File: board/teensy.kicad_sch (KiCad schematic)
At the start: 1 part, among them U2 Teensy4.1_DEV-16771

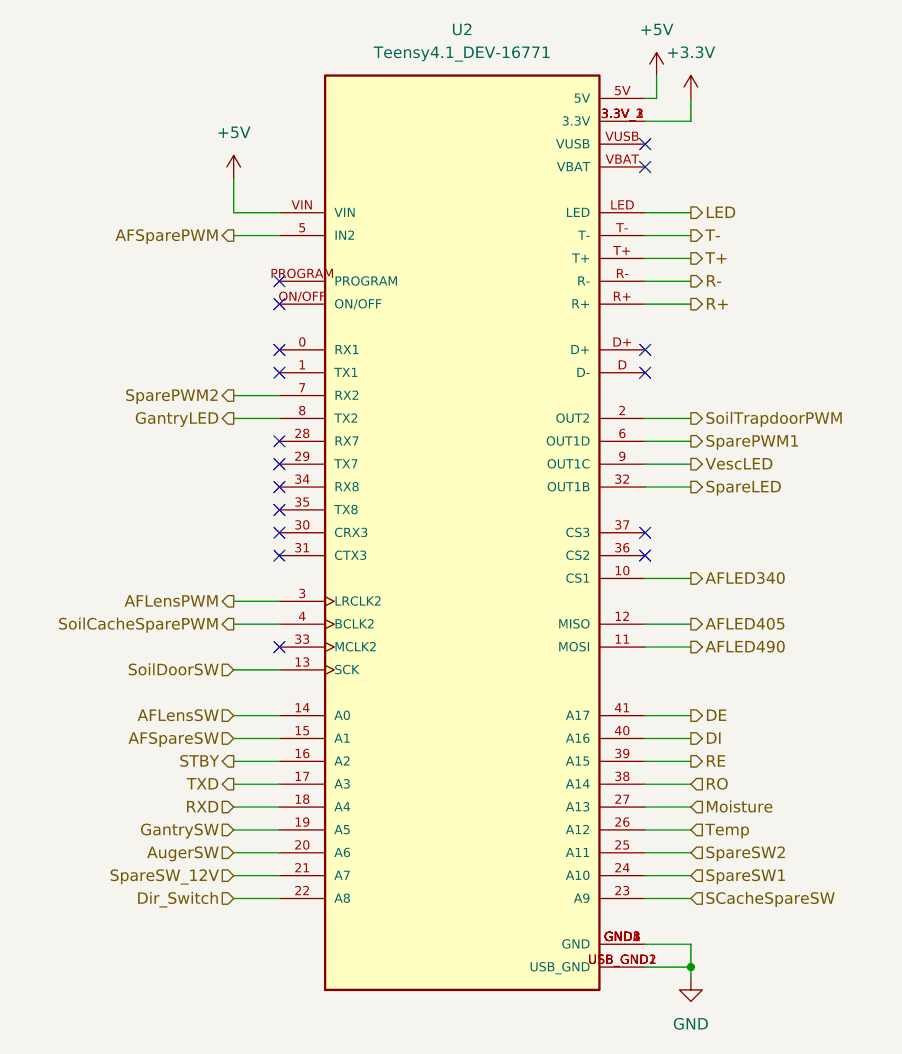
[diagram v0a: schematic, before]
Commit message: Fixed issues after schematic review
added 6 leds for every servo, changed txd and rxd to pins 30/31, added additional oki for 3.3V
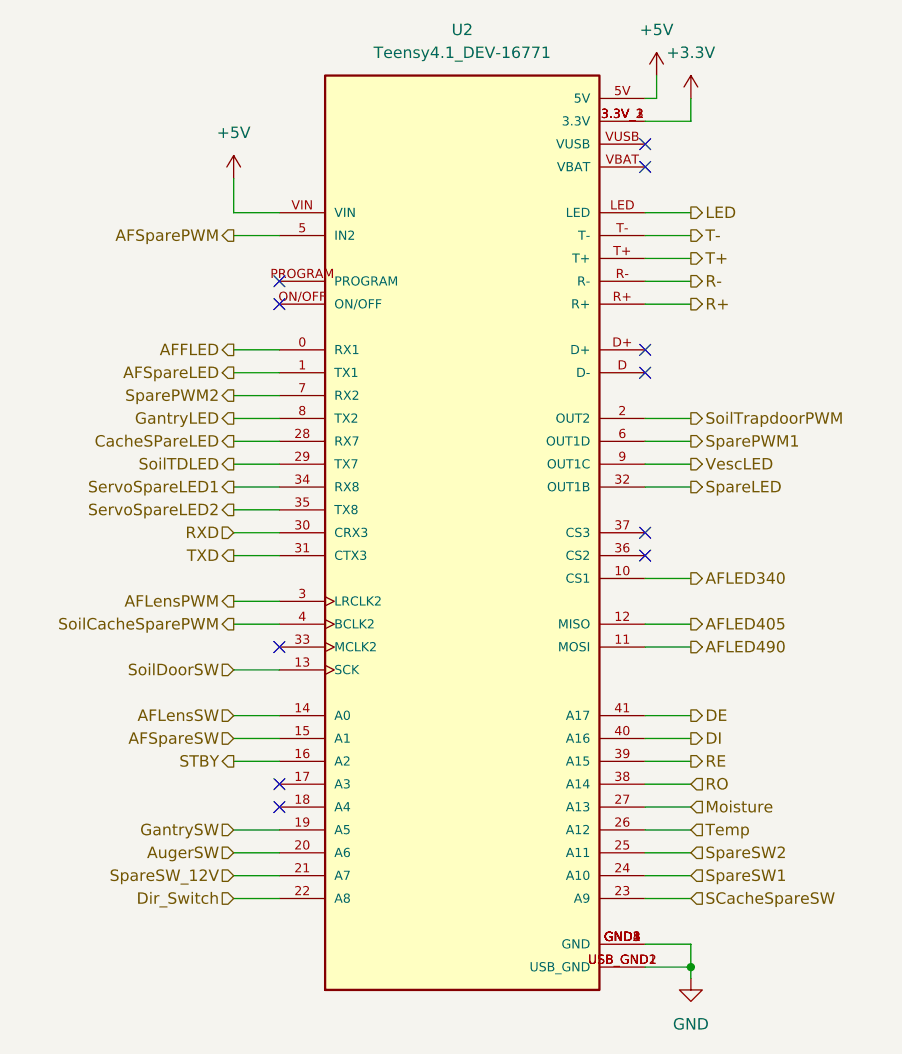
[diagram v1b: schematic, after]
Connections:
- net RXD: now also U2.30 (CRX3); no longer U2.18 (A4)
- net TXD: now also U2.31 (CTX3); no longer U2.17 (A3)
- net AFFLED: now reaches U2.0 (RX1)
- net AFSpareLED: now reaches U2.1 (TX1)
- net CacheSPareLED: now reaches U2.28 (RX7)
- net SoilTDLED: now reaches U2.29 (TX7)
- net ServoSpareLED1: now reaches U2.34 (RX8)
- net ServoSpareLED2: now reaches U2.35 (TX8)
- no-connect marks 17 -> 11
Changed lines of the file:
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@@
 	)
 	(no_connect
-		(at 124.46 71.12)
+		(at 124.46 116.84)
 	)
 	(no_connect
@@
 	)
 	(no_connect
-		(at 124.46 81.28)
-	)
-	(no_connect
 		(at 165.1 68.58)
 	)
@@
 	)
 	(no_connect
-		(at 124.46 91.44)
-	)
-	(no_connect
-		(at 124.46 88.9)
-	)
-	(no_connect
-		(at 124.46 83.82)
-	)
-	(no_connect
 		(at 124.46 60.96)
 	)
@@
 	)
 	(no_connect
+		(at 124.46 119.38)
+	)
+	(no_connect
 		(at 124.46 63.5)
 	)
 	(no_connect
-		(at 124.46 78.74)
-	)
-	(no_connect
 		(at 165.1 88.9)
 	)
 	(no_connect
-		(at 124.46 68.58)
-	)
-	(no_connect
 		(at 124.46 101.6)
 	)
 	(no_connect
-		(at 124.46 86.36)
-	)
-	(no_connect
 		(at 165.1 91.44)
 	)
@@
 	(wire
 		(pts
-			(xy 119.38 119.38) (xy 124.46 119.38)
+			(xy 119.38 91.44) (xy 124.46 91.44)
 		)
 		(stroke
@@
 	(wire
 		(pts
+			(xy 119.38 81.28) (xy 124.46 81.28)
+		)
+		(stroke
+			(width 0)
+			(type default)
+		)
+	)
+	(wire
+		(pts
+			(xy 119.38 71.12) (xy 124.46 71.12)
+		)
+		(stroke
+			(width 0)
+			(type default)
+		)
+	)
+	(wire
+		(pts
+			(xy 119.38 88.9) (xy 124.46 88.9)
+		)
+		(stroke
+			(width 0)
+			(type default)
+		)
+	)
+	(wire
+		(pts
 			(xy 165.1 134.62) (xy 170.18 134.62)
 		)
@@
 	(wire
 		(pts
+			(xy 119.38 68.58) (xy 124.46 68.58)
+		)
+		(stroke
+			(width 0)
+			(type default)
+		)
+	)
+	(wire
+		(pts
+			(xy 119.38 83.82) (xy 124.46 83.82)
+		)
+		(stroke
+			(width 0)
+			(type default)
+		)
+	)
+	(wire
+		(pts
 			(xy 165.1 101.6) (xy 170.18 101.6)
 		)
@@
 	(wire
 		(pts
+			(xy 119.38 78.74) (xy 124.46 78.74)
+		)
+		(stroke
+			(width 0)
+			(type default)
+		)
+	)
+	(wire
+		(pts
 			(xy 165.1 99.06) (xy 170.18 99.06)
 		)
@@
 	(wire
 		(pts
-			(xy 119.38 116.84) (xy 124.46 116.84)
-		)
-		(stroke
-			(width 0)
-			(type default)
-		)
-	)
-	(wire
-		(pts
 			(xy 165.1 121.92) (xy 170.18 121.92)
 		)
@@
 	(wire
 		(pts
+			(xy 119.38 86.36) (xy 124.46 86.36)
+		)
+		(stroke
+			(width 0)
+			(type default)
+		)
+	)
+	(wire
+		(pts
 			(xy 165.1 81.28) (xy 170.18 81.28)
 		)
@@
 		)
 	)
+	(hierarchical_label "SoilTDLED"
+		(shape output)
+		(at 119.38 81.28 180)
+		(effects
+			(font
+				(size 1.27 1.27)
+			)
+			(justify right)
+		)
+	)
 	(hierarchical_label "Temp"
 		(shape input)
@@
 		)
 	)
+	(hierarchical_label "ServoSpareLED1"
+		(shape output)
+		(at 119.38 83.82 180)
+		(effects
+			(font
+				(size 1.27 1.27)
+			)
+			(justify right)
+		)
+	)
 	(hierarchical_label "TXD"
 		(shape output)
-		(at 119.38 116.84 180)
+		(at 119.38 91.44 180)
 		(effects
 			(font
@@
 		)
 	)
+	(hierarchical_label "ServoSpareLED2"
+		(shape output)
+		(at 119.38 86.36 180)
+		(effects
+			(font
+				(size 1.27 1.27)
+			)
+			(justify right)
+		)
+	)
 	(hierarchical_label "SparePWM1"
 		(shape output)
@@
 		)
 	)
+	(hierarchical_label "AFSpareLED"
+		(shape output)
+		(at 119.38 71.12 180)
+		(effects
+			(font
+				(size 1.27 1.27)
+			)
+			(justify right)
+		)
+	)
 	(hierarchical_label "AFSpareSW"
 		(shape input)
@@
 	(hierarchical_label "RXD"
 		(shape input)
-		(at 119.38 119.38 180)
-		(effects
-			(font
+		(at 119.38 88.9 180)
+		(effects
+			(font
+				(size 1.27 1.27)
+			)
+			(justify right)
+		)
+	)
+	(hierarchical_label "AFFLED"
+		(shape output)
+		(at 119.38 68.58 180)
+		(effects
+			(font
+				(size 1.27 1.27)
+			)
+			(justify right)
+		)
+	)
+	(hierarchical_label "CacheSPareLED"
+		(shape output)
+		(at 119.38 78.74 180)
+		(effects
+			(font

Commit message: Edited names and locations for readability
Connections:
- net CacheSPareLED renamed CacheSpareLED
- net SpareLED renamed SpareMotorLED
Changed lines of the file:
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@@
 		)
 	)
-	(hierarchical_label "SpareLED"
+	(hierarchical_label "SpareMotorLED"
 		(shape output)
 		(at 170.18 83.82 0)
@@
 		)
 	)
-	(hierarchical_label "CacheSPareLED"
+	(hierarchical_label "CacheSpareLED"
 		(shape output)
 		(at 119.38 78.74 180)

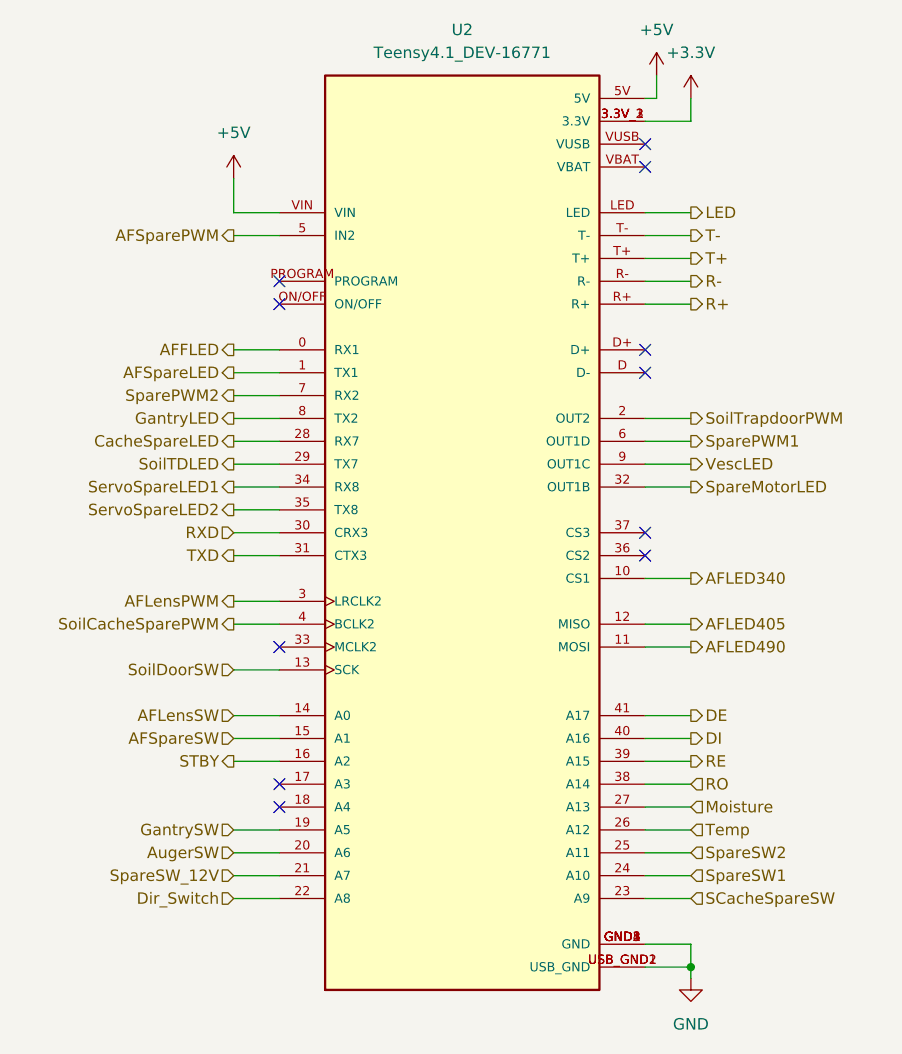
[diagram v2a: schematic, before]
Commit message: Layout Progress
Made a basic setup for locations, placed preliminary wires and text, rearranged teensy pins for simplicity
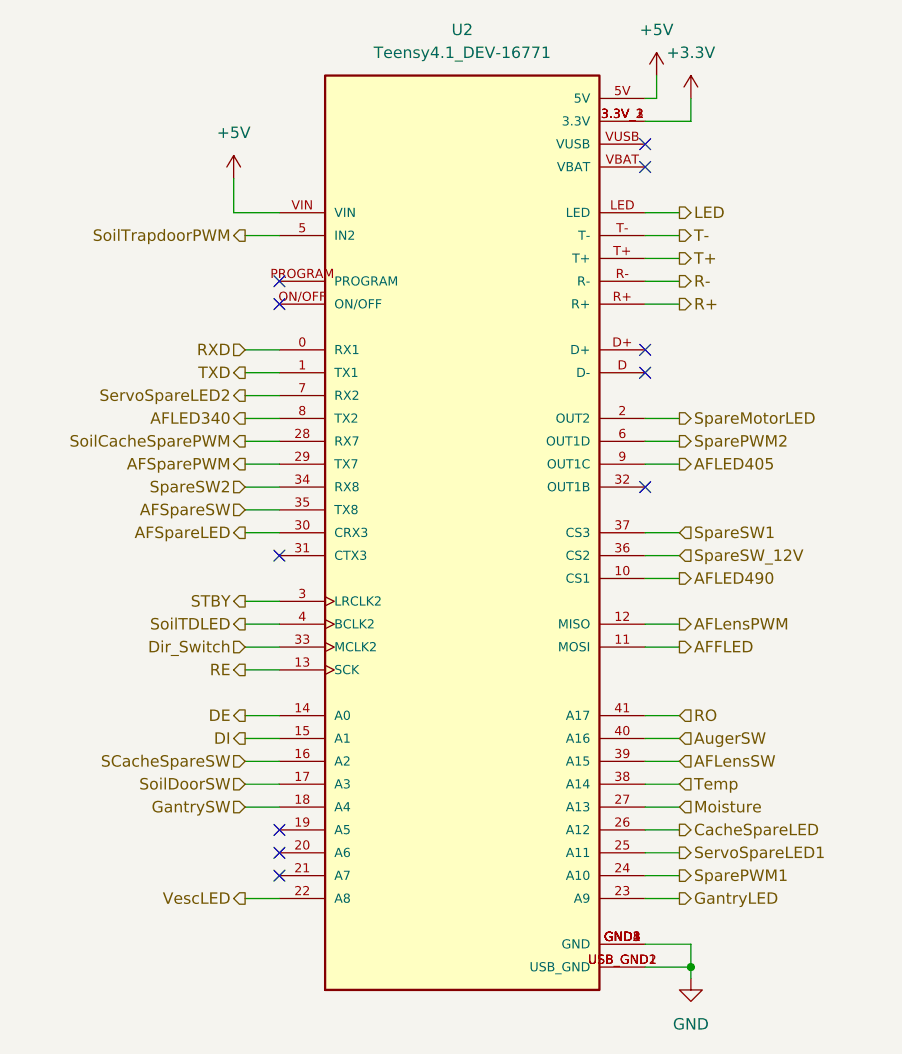
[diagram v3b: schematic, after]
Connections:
- net AFFLED: now also U2.11 (MOSI); no longer U2.0 (RX1)
- net AFLED340: now also U2.8 (TX2); no longer U2.10 (CS1)
- net AFLED405: now also U2.9 (OUT1C); no longer U2.12 (MISO)
- net AFLED490: now also U2.10 (CS1); no longer U2.11 (MOSI)
- net AFLensPWM: now also U2.12 (MISO); no longer U2.3 (LRCLK2)
- net AFLensSW: now also U2.39 (A15); no longer U2.14 (A0)
- net AFSpareLED: now also U2.30 (CRX3); no longer U2.1 (TX1)
- net AFSparePWM: now also U2.29 (TX7); no longer U2.5 (IN2)
- net AFSpareSW: now also U2.35 (TX8); no longer U2.15 (A1)
- net AugerSW: now also U2.40 (A16); no longer U2.20 (A6)
- net CacheSpareLED: now also U2.26 (A12); no longer U2.28 (RX7)
- net DE: now also U2.14 (A0); no longer U2.41 (A17)
- net DI: now also U2.15 (A1); no longer U2.40 (A16)
- net Dir_Switch: now also U2.33 (MCLK2); no longer U2.22 (A8)
- net GantryLED: now also U2.23 (A9); no longer U2.8 (TX2)
- net GantrySW: now also U2.18 (A4); no longer U2.19 (A5)
- net RE: now also U2.13 (SCK); no longer U2.39 (A15)
- net RO: now also U2.41 (A17); no longer U2.38 (A14)
- net RXD: now also U2.0 (RX1); no longer U2.30 (CRX3)
- net SCacheSpareSW: now also U2.16 (A2); no longer U2.23 (A9)
- net STBY: now also U2.3 (LRCLK2); no longer U2.16 (A2)
- net ServoSpareLED1: now also U2.25 (A11); no longer U2.34 (RX8)
- net ServoSpareLED2: now also U2.7 (RX2); no longer U2.35 (TX8)
- net SoilCacheSparePWM: now also U2.28 (RX7); no longer U2.4 (BCLK2)
- net SoilDoorSW: now also U2.17 (A3); no longer U2.13 (SCK)
- net SoilTDLED: now also U2.4 (BCLK2); no longer U2.29 (TX7)
- net SoilTrapdoorPWM: now also U2.5 (IN2); no longer U2.2 (OUT2)
- net SpareMotorLED: now also U2.2 (OUT2); no longer U2.32 (OUT1B)
- net SparePWM1: now also U2.24 (A10); no longer U2.6 (OUT1D)
- net SparePWM2: now also U2.6 (OUT1D); no longer U2.7 (RX2)
- net SpareSW1: now also U2.37 (CS3); no longer U2.24 (A10)
- net SpareSW2: now also U2.34 (RX8); no longer U2.25 (A11)
- net SpareSW_12V: now also U2.36 (CS2); no longer U2.21 (A7)
- net TXD: now also U2.1 (TX1); no longer U2.31 (CTX3)
- net Temp: now also U2.38 (A14); no longer U2.26 (A12)
- net VescLED: now also U2.22 (A8); no longer U2.9 (OUT1C)

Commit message: made minor design changes to layout
changed 12V plane dimensions, rerouted a few traces for clearance
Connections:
- net +5V: no longer U2.5V
- net +3.3V: no longer names the net of U2.3.3V_1 (3.3V), U2.3.3V_2 (3.3V), U2.3.3V_3 (3.3V)
- no-connect marks 11 -> 13
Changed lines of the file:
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@@
+	)
+	(no_connect
+		(at 165.1 43.18)
 	)
 	(no_connect
@@
 		(at 165.1 83.82)
 	)
-	(wire
-		(pts
-			(xy 165.1 40.64) (xy 166.37 40.64)
-		)
-		(stroke
-			(width 0)
-			(type default)
-		)
+	(no_connect
+		(at 165.1 40.64)
 	)
 	(wire
@@
 	(wire
 		(pts
-			(xy 170.18 43.18) (xy 165.1 43.18)
-		)
-		(stroke
-			(width 0)
-			(type default)
-		)
-	)
-	(wire
-		(pts
 			(xy 170.18 137.16) (xy 170.18 138.43)
 		)
@@
 	(wire
 		(pts
-			(xy 170.18 40.64) (xy 170.18 43.18)
-		)
-		(stroke
-			(width 0)
-			(type default)
-		)
-	)
-	(wire
-		(pts
 			(xy 165.1 137.16) (xy 170.18 137.16)
 		)
@@
 		(pts
 			(xy 165.1 55.88) (xy 168.91 55.88)
-		)
-		(stroke
-			(width 0)
-			(type default)
-		)
-	)
-	(wire
-		(pts
-			(xy 166.37 40.64) (xy 166.37 38.1)
 		)
 		(stroke
@@
 					(unit 1)
 				)
-			)
-		)
-	)
-	(symbol
-		(lib_id "power:+3.3V")
-		(at 170.18 40.64 0)
-		(unit 1)
-		(exclude_from_sim no)
-		(in_bom yes)
-		(on_board yes)
-		(dnp no)
-		(fields_autoplaced yes)
-		(property "Reference" "#PWR07"
-			(at 170.18 44.45 0)
-			(effects
-				(font
-					(size 1.27 1.27)
-				)
-				(hide yes)
-			)
-		)
-		(property "Value" "+3.3V"
-			(at 170.18 35.56 0)
-			(effects
-				(font
-					(size 1.27 1.27)
-				)
-			)
-		)
-		(property "Footprint" ""
-			(at 170.18 40.64 0)
-			(effects
-				(font
-					(size 1.27 1.27)
-				)
-				(hide yes)
-			)
-		)
-		(property "Datasheet" ""
-			(at 170.18 40.64 0)
-			(effects
-				(font
-					(size 1.27 1.27)
-				)
-				(hide yes)
-			)
-		)
-		(property "Description" "Power symbol creates a global label with name \"+3.3V\""
-			(at 170.18 40.64 0)
-			(effects
-				(font
-					(size 1.27 1.27)
-				)
-				(hide yes)
-			)
-		)
-		(pin "1"
-		)
-		(instances
-			(project ""
-				(path "/05fd3c2e-b986-4426-9c38-2a77d5c929de/23b17310-6f85-4d9a-8e16-579a52ef7695"
-					(reference "#PWR07")
-					(unit 1)
-				)
-			)
-		)
-	)
-	(symbol
-		(lib_id "power:+5V")
-		(at 166.37 38.1 0)
-		(unit 1)
-		(exclude_from_sim no)
-		(in_bom yes)
-		(on_board yes)
-		(dnp no)
-		(fields_autoplaced yes)
-		(property "Reference" "#PWR064"
-			(at 166.37 41.91 0)
-			(effects
-				(font
-					(size 1.27 1.27)
-				)
-				(hide yes)
-			)
-		)
-		(property "Value" "+5V"
-			(at 166.37 33.02 0)
-			(effects
-				(font
-					(size 1.27 1.27)
-				)
-			)
-		)
-		(property "Footprint" ""
-			(at 166.37 38.1 0)
-			(effects
-				(font
-					(size 1.27 1.27)
-				)
-				(hide yes)
-			)
-		)
-		(property "Datasheet" ""
-			(at 166.37 38.1 0)
-			(effects
-				(font
-					(size 1.27 1.27)
-				)
-				(hide yes)
-			)
-		)
-		(property "Description" "Power symbol creates a global label with name \"+5V\""
-			(at 166.37 38.1 0)
-			(effects
-				(font
-					(size 1.27 1.27)
-				)
-				(hide yes)
-			)
-		)
-		(pin "1"
-		)
-		(instances
-			(project "AugerBoard"
-				(path "/05fd3c2e-b986-4426-9c38-2a77d5c929de/23b17310-6f85-4d9a-8e16-579a52ef7695"
-					(reference "#PWR064")
-					(unit 1)
-				)

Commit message: Added second CAN tranceiver and a switch
also imported a new symbol for both the switch symbol and its footprint
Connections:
- net STBY2: now reaches U2.19 (A5)
- net TXD2: now reaches U2.20 (A6)
- net RXD2: now reaches U2.21 (A7)
- net RXD renamed RXD1
- net STBY renamed STBY1
- net TXD renamed TXD1
- no-connect marks 13 -> 10
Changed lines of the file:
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@@
-	)
-	(no_connect
-		(at 124.46 124.46)
-	)
-	(no_connect
-		(at 124.46 127)
 	)
 	(no_connect
@@
 	)
 	(no_connect
-		(at 124.46 121.92)
-	)
-	(no_connect
 		(at 165.1 68.58)
 	)
@@
 	(wire
 		(pts
+			(xy 120.65 124.46) (xy 124.46 124.46)
+		)
+		(stroke
+			(width 0)
+			(type default)
+		)
+	)
+	(wire
+		(pts
 			(xy 120.65 55.88) (xy 124.46 55.88)
 		)
@@
 	(wire
 		(pts
+			(xy 120.65 127) (xy 124.46 127)
+		)
+		(stroke
+			(width 0)
+			(type default)
+		)
+	)
+	(wire
+		(pts
 			(xy 165.1 124.46) (xy 168.91 124.46)
 		)
@@
 	(wire
 		(pts
+			(xy 120.65 121.92) (xy 124.46 121.92)
+		)
+		(stroke
+			(width 0)
+			(type default)
+		)
+	)
+	(wire
+		(pts
 			(xy 120.65 76.2) (xy 124.46 76.2)
 		)
@@
 		)
 	)
+	(hierarchical_label "RXD2"
+		(shape input)
+		(at 120.65 127 180)
+		(effects
+			(font
+				(size 1.27 1.27)
+			)
+			(justify right)
+		)
+	)
 	(hierarchical_label "SpareSW2"
 		(shape input)
@@
 		)
 	)
-	(hierarchical_label "TXD"
+	(hierarchical_label "TXD1"
 		(shape output)
 		(at 120.65 71.12 180)
@@
 		)
 	)
-	(hierarchical_label "STBY"
+	(hierarchical_label "STBY1"
 		(shape output)
 		(at 120.65 96.52 180)
@@
 		)
 	)
-	(hierarchical_label "RXD"
+	(hierarchical_label "RXD1"
 		(shape input)
 		(at 120.65 68.58 180)
@@
 		)
 	)
+	(hierarchical_label "TXD2"
+		(shape output)
+		(at 120.65 124.46 180)
+		(effects
+			(font
+				(size 1.27 1.27)
+			)
+			(justify right)
+		)
+	)
+	(hierarchical_label "STBY2"
+		(shape output)
+		(at 120.65 121.92 180)
+		(effects
+			(font
+				(size 1.27 1.27)
+			)
+			(justify right)
+		)
+	)
